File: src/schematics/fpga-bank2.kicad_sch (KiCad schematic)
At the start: 7 parts

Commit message: Updates the root page
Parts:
- renumbered C60 to C128, C61 to C129, C62 to C130, C63 to C131, C64 to C132, C65 to C133, U6 to U14
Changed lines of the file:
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@@
 		(dnp no)
 		(fields_autoplaced yes)
-		(property "Reference" "#PWR042"
+		(property "Reference" "#PWR0160"
 			(at 135.89 48.26 0)
 			(effects
@@
 		(instances
 			(project "ecap5-bsom"
-				(path "/c5fd18a3-9aa0-4151-b6e0-94da3d606686/9ec64d27-698a-408d-bb9c-7e381193a80d/8bbad842-d59a-4b95-b8ee-3131df68465b"
-					(reference "#PWR042")
+				(path "/c5fd18a3-9aa0-4151-b6e0-94da3d606686/82eaa538-a5ac-465e-a467-f81a7248ecaa"
+					(reference "#PWR0160")
 					(unit 1)
 				)
@@
 		(dnp no)
 		(fields_autoplaced yes)
-		(property "Reference" "#PWR039"
+		(property "Reference" "#PWR0157"
 			(at 115.57 34.29 0)
 			(effects
@@
 		(instances
 			(project "ecap5-bsom"
-				(path "/c5fd18a3-9aa0-4151-b6e0-94da3d606686/9ec64d27-698a-408d-bb9c-7e381193a80d/8bbad842-d59a-4b95-b8ee-3131df68465b"
-					(reference "#PWR039")
+				(path "/c5fd18a3-9aa0-4151-b6e0-94da3d606686/82eaa538-a5ac-465e-a467-f81a7248ecaa"
+					(reference "#PWR0157")
 					(unit 1)
 				)
@@
 		(dnp no)
 		(fields_autoplaced yes)
-		(property "Reference" "C60"
+		(property "Reference" "C128"
 			(at 113.03 36.8362 0)
 			(effects
@@
 		(instances
 			(project "ecap5-bsom"
-				(path "/c5fd18a3-9aa0-4151-b6e0-94da3d606686/9ec64d27-698a-408d-bb9c-7e381193a80d/8bbad842-d59a-4b95-b8ee-3131df68465b"
-					(reference "C60")
+				(path "/c5fd18a3-9aa0-4151-b6e0-94da3d606686/82eaa538-a5ac-465e-a467-f81a7248ecaa"
+					(reference "C128")
 					(unit 1)
 				)
@@
 		(dnp no)
 		(fields_autoplaced yes)
-		(property "Reference" "C62"
+		(property "Reference" "C130"
 			(at 133.35 36.8362 0)
 			(effects
@@
 		(instances
 			(project "ecap5-bsom"
-				(path "/c5fd18a3-9aa0-4151-b6e0-94da3d606686/9ec64d27-698a-408d-bb9c-7e381193a80d/8bbad842-d59a-4b95-b8ee-3131df68465b"
-					(reference "C62")
+				(path "/c5fd18a3-9aa0-4151-b6e0-94da3d606686/82eaa538-a5ac-465e-a467-f81a7248ecaa"
+					(reference "C130")
 					(unit 1)
 				)
@@
 		(dnp no)
 		(fields_autoplaced yes)
-		(property "Reference" "C65"
+		(property "Reference" "C133"
 			(at 165.1 36.8362 0)
 			(effects
@@
 		(instances
 			(project "ecap5-bsom"
-				(path "/c5fd18a3-9aa0-4151-b6e0-94da3d606686/9ec64d27-698a-408d-bb9c-7e381193a80d/8bbad842-d59a-4b95-b8ee-3131df68465b"
-					(reference "C65")
+				(path "/c5fd18a3-9aa0-4151-b6e0-94da3d606686/82eaa538-a5ac-465e-a467-f81a7248ecaa"
+					(reference "C133")
 					(unit 1)
 				)
@@
 		(dnp no)
 		(fields_autoplaced yes)
-		(property "Reference" "#PWR043"
+		(property "Reference" "#PWR0161"
 			(at 146.05 48.26 0)
 			(effects
@@
 		(instances
 			(project "ecap5-bsom"
-				(path "/c5fd18a3-9aa0-4151-b6e0-94da3d606686/9ec64d27-698a-408d-bb9c-7e381193a80d/8bbad842-d59a-4b95-b8ee-3131df68465b"
-					(reference "#PWR043")
+				(path "/c5fd18a3-9aa0-4151-b6e0-94da3d606686/82eaa538-a5ac-465e-a467-f81a7248ecaa"
+					(reference "#PWR0161")
 					(unit 1)
 				)
@@
 		(dnp no)
 		(fields_autoplaced yes)
-		(property "Reference" "#PWR045"
+		(property "Reference" "#PWR0163"
 			(at 167.64 48.26 0)
 			(effects
@@
 		(instances
 			(project "ecap5-bsom"
-				(path "/c5fd18a3-9aa0-4151-b6e0-94da3d606686/9ec64d27-698a-408d-bb9c-7e381193a80d/8bbad842-d59a-4b95-b8ee-3131df68465b"
-					(reference "#PWR045")
+				(path "/c5fd18a3-9aa0-4151-b6e0-94da3d606686/82eaa538-a5ac-465e-a467-f81a7248ecaa"
+					(reference "#PWR0163")
 					(unit 1)
 				)
@@
 		(on_board yes)
 		(dnp no)
-		(property "Reference" "U6"
+		(property "Reference" "U14"
 			(at 141.732 71.2469 0)
 			(effects
@@
 		(instances
 			(project "ecap5-bsom"
-				(path "/c5fd18a3-9aa0-4151-b6e0-94da3d606686/9ec64d27-698a-408d-bb9c-7e381193a80d/8bbad842-d59a-4b95-b8ee-3131df68465b"
-					(reference "U6")
+				(path "/c5fd18a3-9aa0-4151-b6e0-94da3d606686/82eaa538-a5ac-465e-a467-f81a7248ecaa"
+					(reference "U14")
 					(unit 4)
 				)
@@
 		(dnp no)
 		(fields_autoplaced yes)
-		(property "Reference" "C64"
+		(property "Reference" "C132"
 			(at 153.67 36.8362 0)
 			(effects
@@
 		(instances
 			(project "ecap5-bsom"
-				(path "/c5fd18a3-9aa0-4151-b6e0-94da3d606686/9ec64d27-698a-408d-bb9c-7e381193a80d/8bbad842-d59a-4b95-b8ee-3131df68465b"
-					(reference "C64")
+				(path "/c5fd18a3-9aa0-4151-b6e0-94da3d606686/82eaa538-a5ac-465e-a467-f81a7248ecaa"
+					(reference "C132")
 					(unit 1)
 				)
@@
 		(dnp no)
 		(fields_autoplaced yes)
-		(property "Reference" "#PWR044"
+		(property "Reference" "#PWR0162"
 			(at 156.21 48.26 0)
 			(effects
@@
 		(instances
 			(project "ecap5-bsom"
-				(path "/c5fd18a3-9aa0-4151-b6e0-94da3d606686/9ec64d27-698a-408d-bb9c-7e381193a80d/8bbad842-d59a-4b95-b8ee-3131df68465b"
-					(reference "#PWR044")
+				(path "/c5fd18a3-9aa0-4151-b6e0-94da3d606686/82eaa538-a5ac-465e-a467-f81a7248ecaa"
+					(reference "#PWR0162")
 					(unit 1)
 				)
@@
 		(dnp no)
 		(fields_autoplaced yes)
-		(property "Reference" "C61"
+		(property "Reference" "C129"
 			(at 123.19 36.8362 0)
 			(effects
@@
 		(instances
 			(project "ecap5-bsom"
-				(path "/c5fd18a3-9aa0-4151-b6e0-94da3d606686/9ec64d27-698a-408d-bb9c-7e381193a80d/8bbad842-d59a-4b95-b8ee-3131df68465b"
-					(reference "C61")
+				(path "/c5fd18a3-9aa0-4151-b6e0-94da3d606686/82eaa538-a5ac-465e-a467-f81a7248ecaa"
+					(reference "C129")
 					(unit 1)
 				)
@@
 		(dnp no)
 		(fields_autoplaced yes)
-		(property "Reference" "C63"
+		(property "Reference" "C131"
 			(at 143.51 36.8362 0)
 			(effects
@@
 		(instances
 			(project "ecap5-bsom"
-				(path "/c5fd18a3-9aa0-4151-b6e0-94da3d606686/9ec64d27-698a-408d-bb9c-7e381193a80d/8bbad842-d59a-4b95-b8ee-3131df68465b"
-					(reference "C63")
+				(path "/c5fd18a3-9aa0-4151-b6e0-94da3d606686/82eaa538-a5ac-465e-a467-f81a7248ecaa"
+					(reference "C131")
 					(unit 1)
 				)
@@
 		(dnp no)
 		(fields_autoplaced yes)
-		(property "Reference" "#PWR040"
+		(property "Reference" "#PWR0158"
 			(at 115.57 48.26 0)
 			(effects
@@
 		(instances
 			(project "ecap5-bsom"
-				(path "/c5fd18a3-9aa0-4151-b6e0-94da3d606686/9ec64d27-698a-408d-bb9c-7e381193a80d/8bbad842-d59a-4b95-b8ee-3131df68465b"
-					(reference "#PWR040")
+				(path "/c5fd18a3-9aa0-4151-b6e0-94da3d606686/82eaa538-a5ac-465e-a467-f81a7248ecaa"
+					(reference "#PWR0158")
 					(unit 1)
 				)
@@
 		(dnp no)
 		(fields_autoplaced yes)
-		(property "Reference" "#PWR041"
+		(property "Reference" "#PWR0159"
 			(at 125.73 48.26 0)
 			(effects
@@
 		(instances
 			(project "ecap5-bsom"
-				(path "/c5fd18a3-9aa0-4151-b6e0-94da3d606686/9ec64d27-698a-408d-bb9c-7e381193a80d/8bbad842-d59a-4b95-b8ee-3131df68465b"
-					(reference "#PWR041")
+				(path "/c5fd18a3-9aa0-4151-b6e0-94da3d606686/82eaa538-a5ac-465e-a467-f81a7248ecaa"
+					(reference "#PWR0159")
 					(unit 1)
 				)

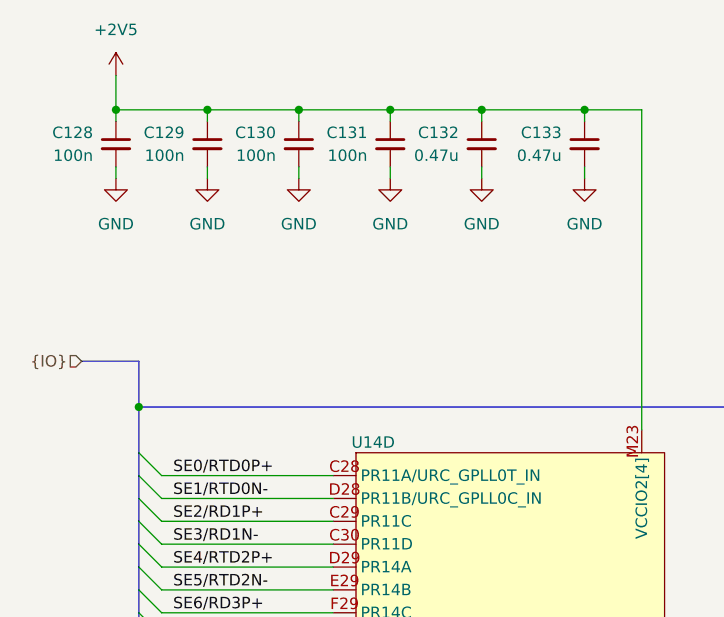
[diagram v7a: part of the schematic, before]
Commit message: Fixes ERC issues
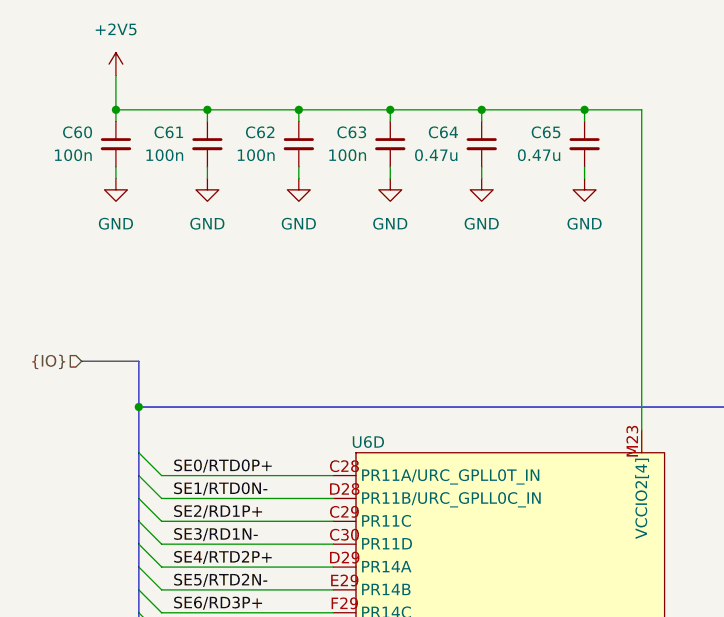
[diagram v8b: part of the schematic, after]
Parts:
- renumbered C128 to C60, C129 to C61, C130 to C62, C131 to C63, C132 to C64, C133 to C65, U14 to U6
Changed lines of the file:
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@@
 		(dnp no)
 		(fields_autoplaced yes)
-		(property "Reference" "#PWR0160"
+		(property "Reference" "#PWR043"
 			(at 135.89 48.26 0)
 			(effects
@@
 			(project "ecap5-bsom"
 				(path "/c5fd18a3-9aa0-4151-b6e0-94da3d606686/82eaa538-a5ac-465e-a467-f81a7248ecaa"
-					(reference "#PWR0160")
+					(reference "#PWR043")
 					(unit 1)
 				)
@@
 		(dnp no)
 		(fields_autoplaced yes)
-		(property "Reference" "#PWR0157"
+		(property "Reference" "#PWR040"
 			(at 115.57 34.29 0)
 			(effects
@@
 			(project "ecap5-bsom"
 				(path "/c5fd18a3-9aa0-4151-b6e0-94da3d606686/82eaa538-a5ac-465e-a467-f81a7248ecaa"
-					(reference "#PWR0157")
+					(reference "#PWR040")
 					(unit 1)
 				)
@@
 		(dnp no)
 		(fields_autoplaced yes)
-		(property "Reference" "C128"
+		(property "Reference" "C60"
 			(at 113.03 36.8362 0)
 			(effects
@@
 			(project "ecap5-bsom"
 				(path "/c5fd18a3-9aa0-4151-b6e0-94da3d606686/82eaa538-a5ac-465e-a467-f81a7248ecaa"
-					(reference "C128")
+					(reference "C60")
 					(unit 1)
 				)
@@
 		(dnp no)
 		(fields_autoplaced yes)
-		(property "Reference" "C130"
+		(property "Reference" "C62"
 			(at 133.35 36.8362 0)
 			(effects
@@
 			(project "ecap5-bsom"
 				(path "/c5fd18a3-9aa0-4151-b6e0-94da3d606686/82eaa538-a5ac-465e-a467-f81a7248ecaa"
-					(reference "C130")
+					(reference "C62")
 					(unit 1)
 				)
@@
 		(dnp no)
 		(fields_autoplaced yes)
-		(property "Reference" "C133"
+		(property "Reference" "C65"
 			(at 165.1 36.8362 0)
 			(effects
@@
 			(project "ecap5-bsom"
 				(path "/c5fd18a3-9aa0-4151-b6e0-94da3d606686/82eaa538-a5ac-465e-a467-f81a7248ecaa"
-					(reference "C133")
+					(reference "C65")
 					(unit 1)
 				)
@@
 		(dnp no)
 		(fields_autoplaced yes)
-		(property "Reference" "#PWR0161"
+		(property "Reference" "#PWR044"
 			(at 146.05 48.26 0)
 			(effects
@@
 			(project "ecap5-bsom"
 				(path "/c5fd18a3-9aa0-4151-b6e0-94da3d606686/82eaa538-a5ac-465e-a467-f81a7248ecaa"
-					(reference "#PWR0161")
+					(reference "#PWR044")
 					(unit 1)
 				)
@@
 		(dnp no)
 		(fields_autoplaced yes)
-		(property "Reference" "#PWR0163"
+		(property "Reference" "#PWR046"
 			(at 167.64 48.26 0)
 			(effects
@@
 			(project "ecap5-bsom"
 				(path "/c5fd18a3-9aa0-4151-b6e0-94da3d606686/82eaa538-a5ac-465e-a467-f81a7248ecaa"
-					(reference "#PWR0163")
+					(reference "#PWR046")
 					(unit 1)
 				)
@@
 		(on_board yes)
 		(dnp no)
-		(property "Reference" "U14"
+		(property "Reference" "U6"
 			(at 141.732 71.2469 0)
 			(effects
@@
 			(project "ecap5-bsom"
 				(path "/c5fd18a3-9aa0-4151-b6e0-94da3d606686/82eaa538-a5ac-465e-a467-f81a7248ecaa"
-					(reference "U14")
+					(reference "U6")
 					(unit 4)
 				)
@@
 		(dnp no)
 		(fields_autoplaced yes)
-		(property "Reference" "C132"
+		(property "Reference" "C64"
 			(at 153.67 36.8362 0)
 			(effects
@@
 			(project "ecap5-bsom"
 				(path "/c5fd18a3-9aa0-4151-b6e0-94da3d606686/82eaa538-a5ac-465e-a467-f81a7248ecaa"
-					(reference "C132")
+					(reference "C64")
 					(unit 1)
 				)
@@
 		(dnp no)
 		(fields_autoplaced yes)
-		(property "Reference" "#PWR0162"
+		(property "Reference" "#PWR045"
 			(at 156.21 48.26 0)
 			(effects
@@
 			(project "ecap5-bsom"
 				(path "/c5fd18a3-9aa0-4151-b6e0-94da3d606686/82eaa538-a5ac-465e-a467-f81a7248ecaa"
-					(reference "#PWR0162")
+					(reference "#PWR045")
 					(unit 1)
 				)
@@
 		(dnp no)
 		(fields_autoplaced yes)
-		(property "Reference" "C129"
+		(property "Reference" "C61"
 			(at 123.19 36.8362 0)
 			(effects
@@
 			(project "ecap5-bsom"
 				(path "/c5fd18a3-9aa0-4151-b6e0-94da3d606686/82eaa538-a5ac-465e-a467-f81a7248ecaa"
-					(reference "C129")
+					(reference "C61")
 					(unit 1)
 				)
@@
 		(dnp no)
 		(fields_autoplaced yes)
-		(property "Reference" "C131"
+		(property "Reference" "C63"
 			(at 143.51 36.8362 0)
 			(effects
@@
 			(project "ecap5-bsom"
 				(path "/c5fd18a3-9aa0-4151-b6e0-94da3d606686/82eaa538-a5ac-465e-a467-f81a7248ecaa"
-					(reference "C131")
+					(reference "C63")
 					(unit 1)
 				)
@@
 		(dnp no)
 		(fields_autoplaced yes)
-		(property "Reference" "#PWR0158"
+		(property "Reference" "#PWR041"
 			(at 115.57 48.26 0)
 			(effects
@@
 			(project "ecap5-bsom"
 				(path "/c5fd18a3-9aa0-4151-b6e0-94da3d606686/82eaa538-a5ac-465e-a467-f81a7248ecaa"
-					(reference "#PWR0158")
+					(reference "#PWR041")
 					(unit 1)
 				)
@@
 		(dnp no)
 		(fields_autoplaced yes)
-		(property "Reference" "#PWR0159"
+		(property "Reference" "#PWR042"
 			(at 125.73 48.26 0)
 			(effects
@@
 			(project "ecap5-bsom"
 				(path "/c5fd18a3-9aa0-4151-b6e0-94da3d606686/82eaa538-a5ac-465e-a467-f81a7248ecaa"
-					(reference "#PWR0159")
+					(reference "#PWR042")
 					(unit 1)
 				)
